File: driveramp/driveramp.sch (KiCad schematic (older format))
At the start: 91 parts, among them J1 SMA, J2 SMA, K1 CONN_3, K2 CONN_3, P2 CONN_2, Q1 BC547BTA, T1 MABACT0067, T2 2x Fair-Rite 2843006802, coax, U1 DG9411, U2 MRFE6VP100H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

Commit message: moved rf amps from control board to rxfe and driver
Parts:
- removed C1, C3: DNP, SMD_Packages:SMD-1210, symbol C
- removed C2: JMP, SMD_Packages:SMD-1210, symbol C
- removed C28, C39, C9: 100 nF, SMD_Packages:SMD-0805, symbol C
- removed K2: CONN_3, localconn:3-647166-3, symbol CONN_3
- removed R17, R18: DNP, SMD_Packages:SMD-0805, symbol R
- removed R19: 20, SMD_Packages:SMD-0805, symbol R
- removed R20: 52.3K 1%, SMD_Packages:SMD-0603, symbol R
- removed R21: 10K 1%, SMD_Packages:SMD-0603, symbol R
- removed R22: 10k, SMD_Packages:SMD-0603, symbol R
- removed U5: LT3010EMS8E, local:MSOP8-EP, symbol LT3010EMS8E
- added C? (x2): 22nF, SMD_Packages:SMD-0805, symbol C
- added C?: 100 nF, SMD_Packages:SMD-0805, symbol C
- added JP?: JUMPER3, symbol JUMPER3
- added L?: 1.5 uH, SMD_Packages:SM1812, symbol INDUCTOR
- added R?: 43.2, SMD_Packages:SM2512, symbol R
- added U?: GALI6+, symbol HMC475
- added U?: LM2937, symbol LM2937
- C20, C22: value 22nF -> DNP
- C24: value 100 pF -> 22 pF
- C26: value 10 nF -> 22 nF
- C38: value 1uF -> 10 uF
- C40: value 1uF 100V -> 100 nF
- R14: value 10k 1% -> 10k
- R15: value 1.5 -> 5.1
- R5: value 100k -> 10k
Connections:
- net labels added: VPP
- wire segments 197 -> 183
- no-connect marks 1 -> 0
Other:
- note added: "add GALI 6+ (12.2 dB gain)\nRemove amplifier from control board, cut bias on driver amp\nadd 15V input"
- note added: "jumper to \nselect pulsed/cw bias"
- note removed: "mouser cart:\nhttp://www.mouser.com/ProjectManager/ProjectDetail.aspx?AccessID=78a24cbee4\n\nDigikey: \nWeb ID 106262028 Access ID 70481"
- moved on the sheet: C38, C40, J1, L4, R16

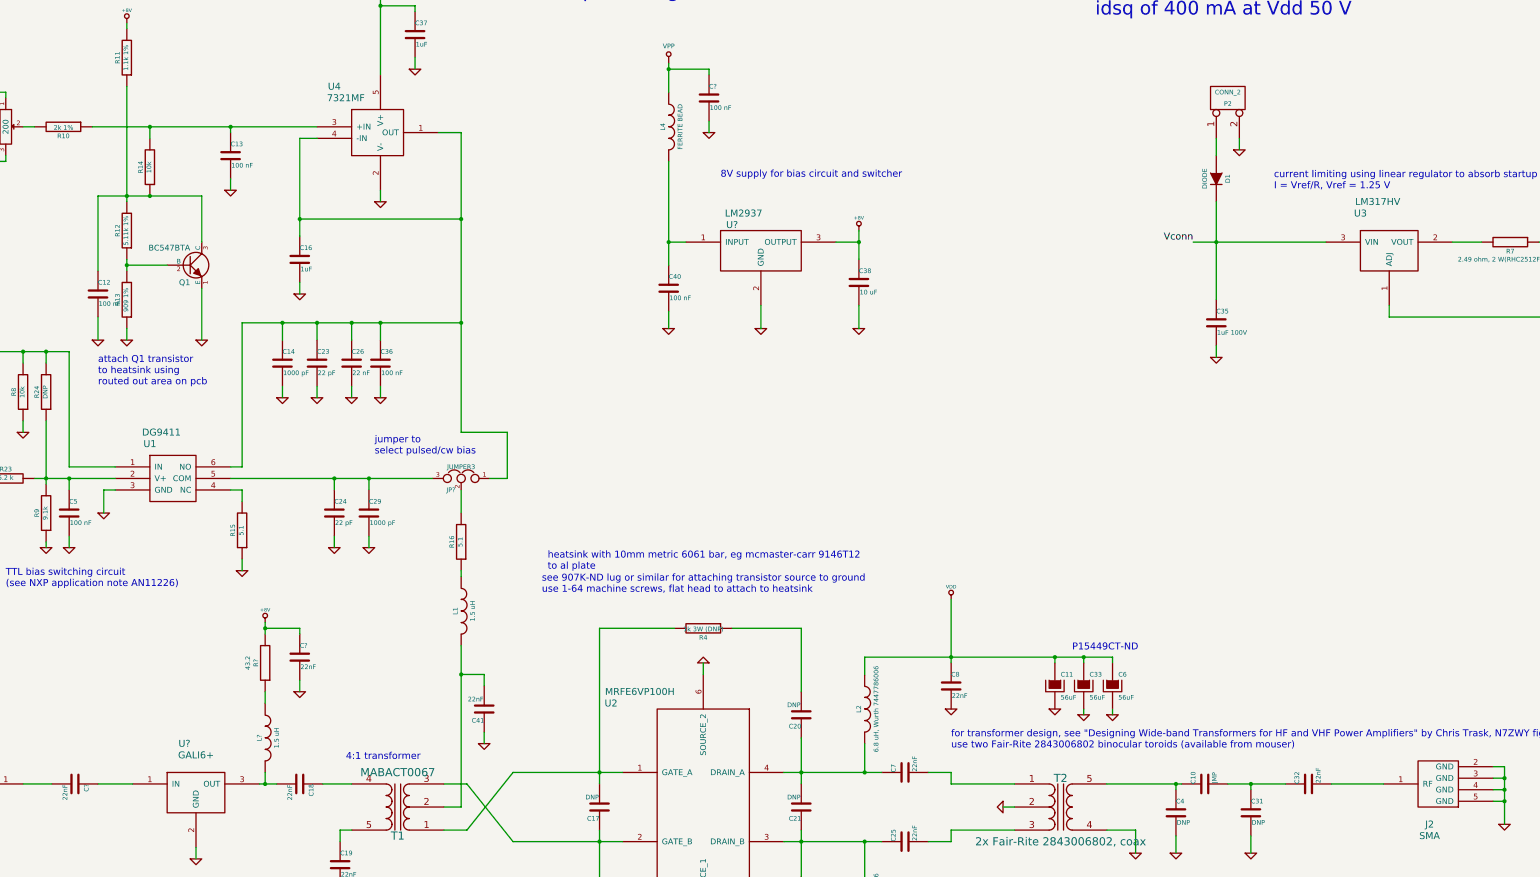
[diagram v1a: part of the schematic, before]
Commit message: DFM changes to boards - added fiducial markers and increase paste clearance
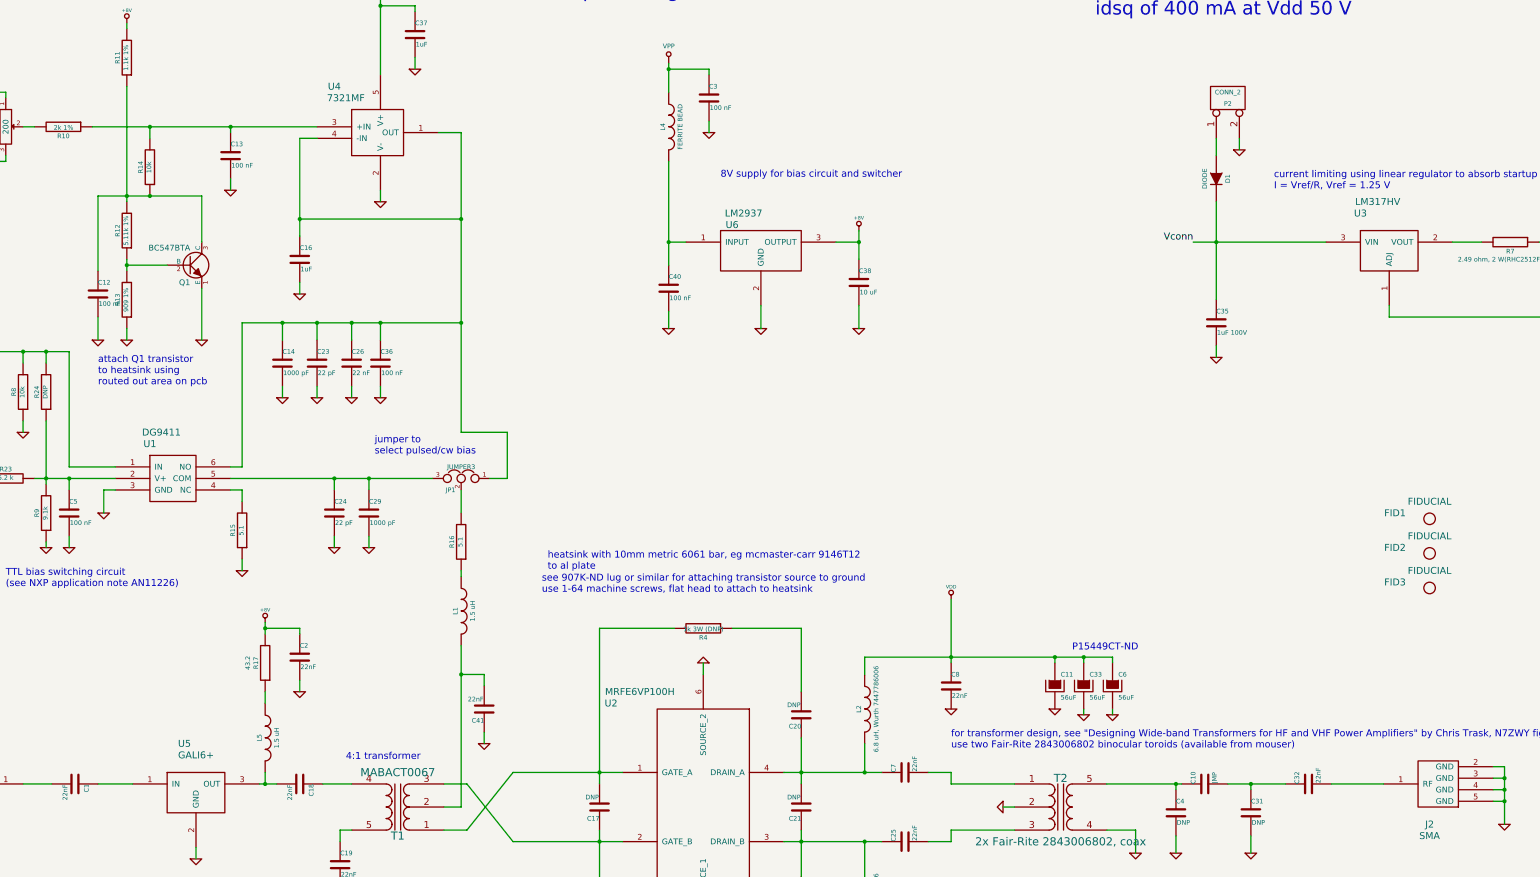
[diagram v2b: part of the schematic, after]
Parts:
- added FID1, FID2, FID3: FIDUCIAL, Mounting_Holes:MountingHole_2-7mm, symbol MOUNTING_HOLE
- gave numbers to parts that had none: 8

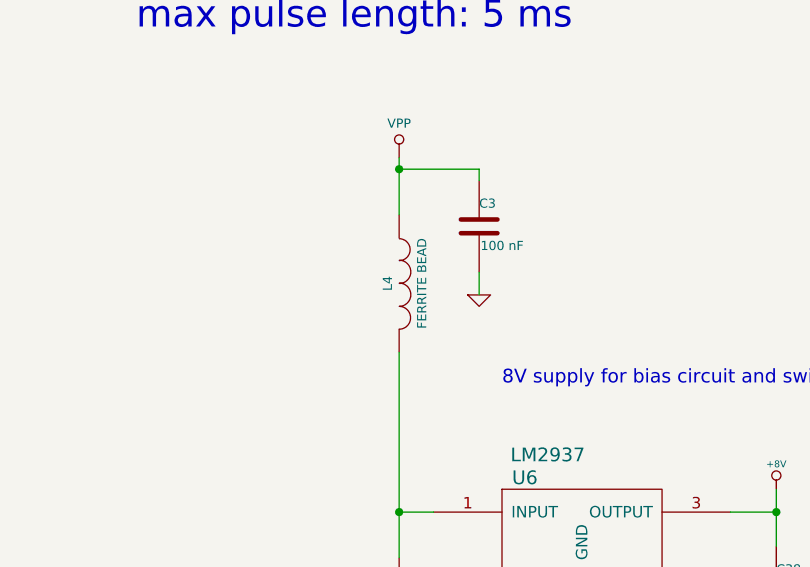
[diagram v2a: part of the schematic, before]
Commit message: finished layout of DFM'ed driver ampifier board.. except still need to change connectors
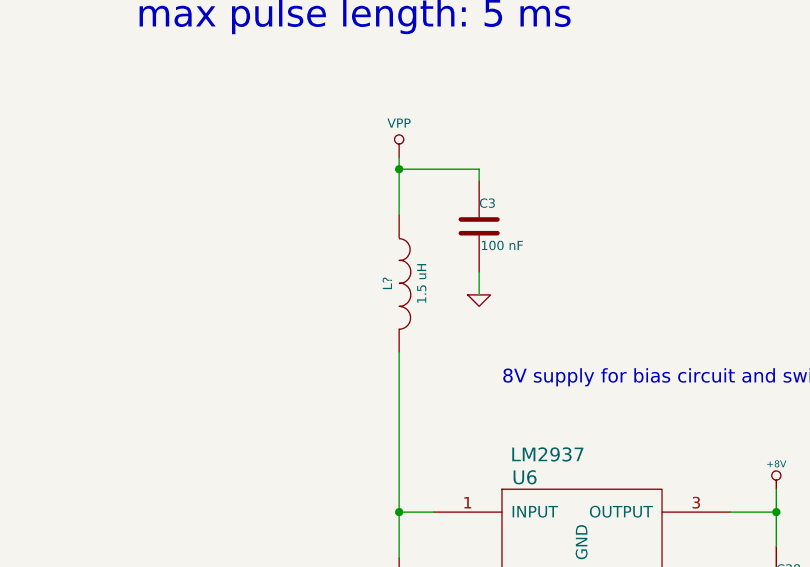
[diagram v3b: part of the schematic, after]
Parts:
- removed L4: FERRITE BEAD, SMD_Packages:SMD-0805, symbol INDUCTOR
- added L?: 1.5 uH, SMD_Packages:SMD-1812, symbol INDUCTOR
- C4: footprint SMD_Packages:SMD-1210 -> SMD_Packages:SMD-0805
- FID1, FID2, FID3: footprint Mounting_Holes:MountingHole_2-7mm -> sdtransmitter:FID_1MM
- JP1: footprint (none) -> localconn:3-647166-3
- L5: footprint SMD_Packages:SM1812 -> SMD_Packages:SMD-1812
- R17: footprint SMD_Packages:SM2512 -> SMD_Packages:SMD-0805
- U5: footprint (none) -> Housings_SOT-89:SOT89-3_Housing
- U6: footprint (none) -> SMD_Packages:SOT-223
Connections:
- net VPP: now also L?.1
- net at C40.1, U6.1 (INPUT): now also L?.2

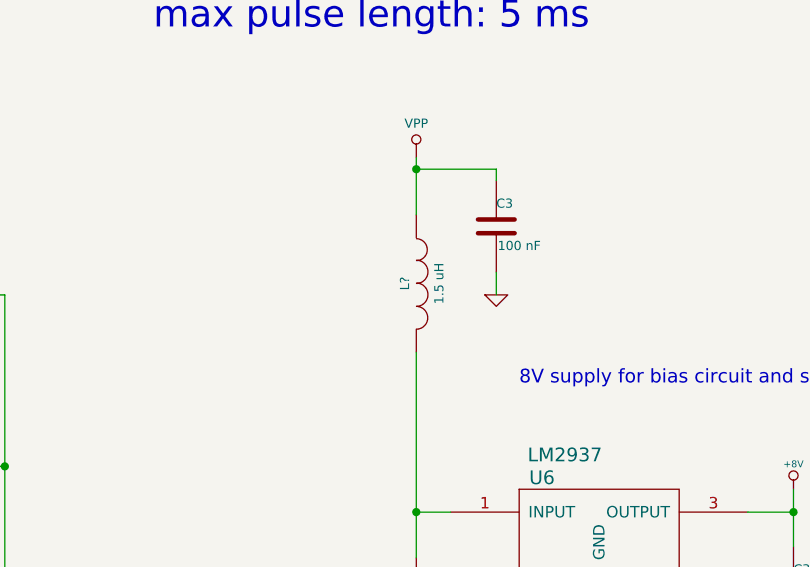
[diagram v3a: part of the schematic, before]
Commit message: changed all 3 pin headers to molex smd connectors available in tube packaging..
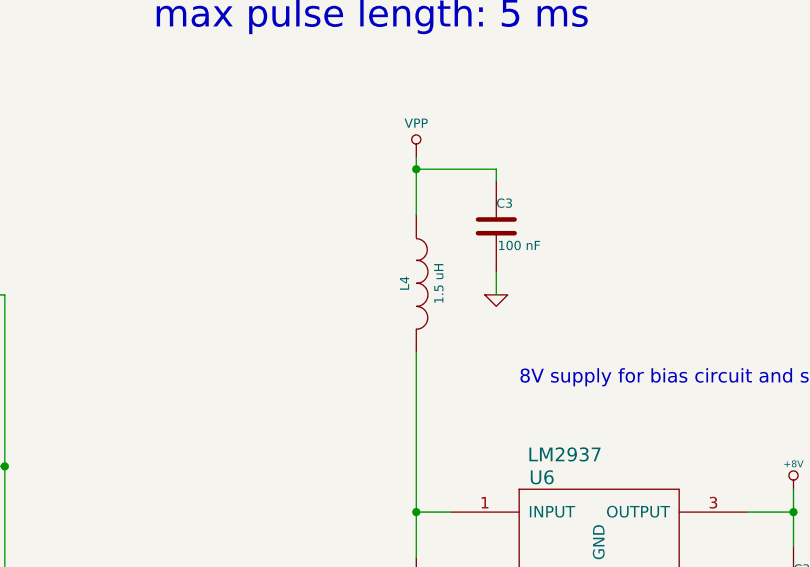
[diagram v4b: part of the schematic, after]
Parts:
- gave numbers to parts that had none: 1

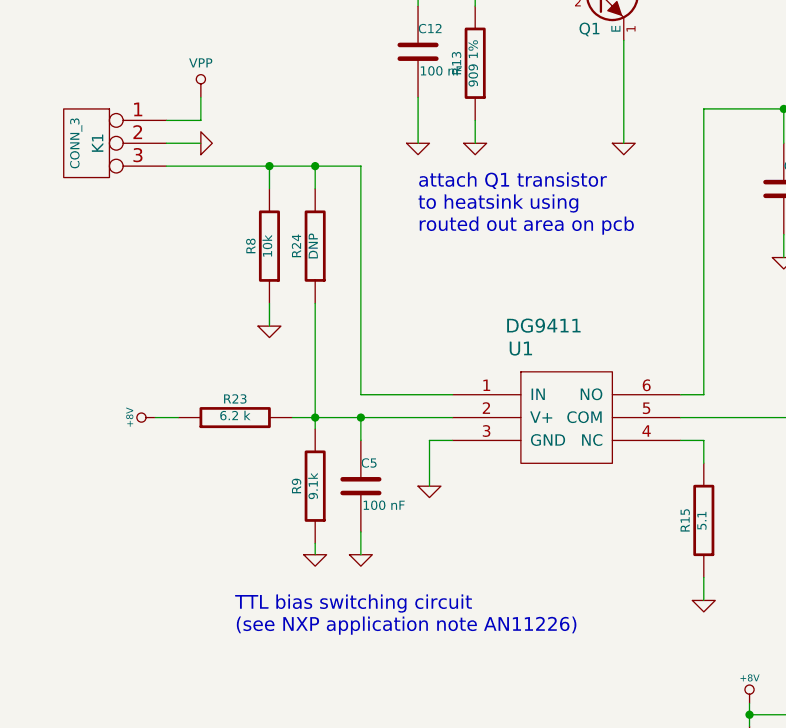
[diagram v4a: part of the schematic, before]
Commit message: rearranged high power T/R switch to place all connectors on one side for easier mounting to cases
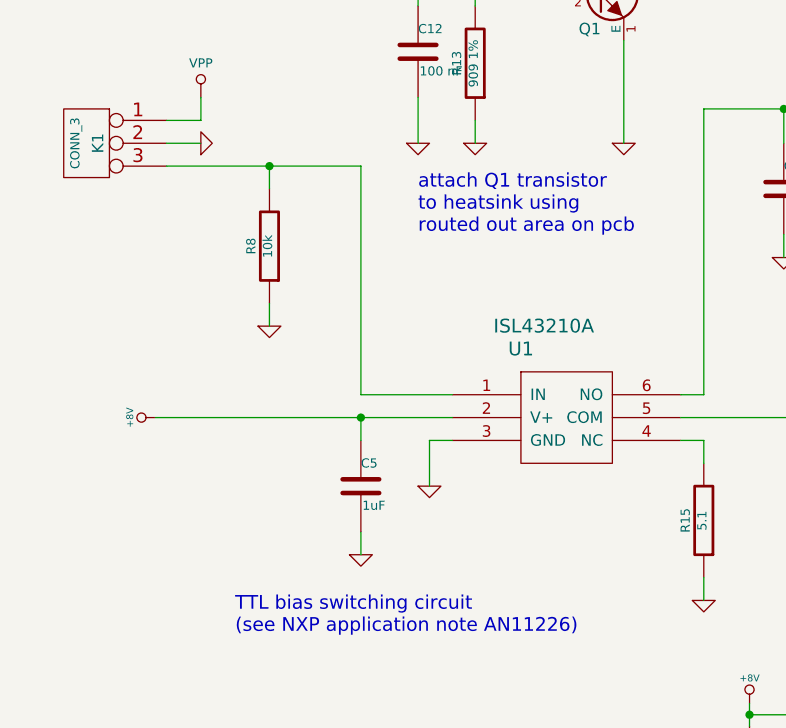
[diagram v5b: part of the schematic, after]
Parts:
- removed R23: 6.2 k, SMD_Packages:SMD-0603, symbol R
- removed R24: DNP, SMD_Packages:SMD-0603, symbol R
- removed R9: 9.1k, SMD_Packages:SMD-0603, symbol R
- C5: value 100 nF -> 1uF
- U1: value DG9411 -> ISL43210A
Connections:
- net +8V: now also C5.1, U1.2 (V+)
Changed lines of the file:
@@
 P 2900 5100
 F 0 "U1" H 2700 5400 60  0000 C CNN
-F 1 "DG9411" H 2800 5500 60  0000 C CNN
+F 1 "ISL43210A" H 2800 5500 60  0000 C CNN
 F 2 "Transistors_SMD:sc70-6" H 2900 5100 60  0001 C CNN
 F 3 "" H 2900 5100 60  0000 C CNN
@@
 P 2000 5400
 F 0 "C5" H 2000 5500 40  0000 L CNN
-F 1 "100 nF" H 2006 5315 40  0000 L CNN
+F 1 "1uF" H 2006 5315 40  0000 L CNN
 F 2 "SMD_Packages:SMD-0805" H 2038 5250 30  0001 C CNN
 F 3 "~" H 2000 5400 60  0000 C CNN
@@
 	1    2000 5700
 	1    0    0    -1
-$EndComp
-$Comp
-L R R9
-U 1 1 54ACADEE
-P 1800 5400
-F 0 "R9" V 1880 5400 40  0000 C CNN
-F 1 "9.1k" V 1807 5401 40  0000 C CNN
-F 2 "SMD_Packages:SMD-0603" V 1730 5400 30  0001 C CNN
-F 3 "" H 1800 5400 30  0000 C CNN
-	1    1800 5400
-	-1   0    0    1
-$EndComp
-$Comp
-L GND #PWR8
-U 1 1 54ACADF9
-P 1800 5700
-F 0 "#PWR8" H 1800 5700 30  0001 C CNN
-F 1 "GND" H 1800 5630 30  0001 C CNN
-F 2 "" H 1800 5700 60  0000 C CNN
-F 3 "" H 1800 5700 60  0000 C CNN
-	1    1800 5700
-	1    0    0    -1
-$EndComp
-$Comp
-L R R23
-U 1 1 54ACB329
-P 1450 5100
-F 0 "R23" V 1530 5100 40  0000 C CNN
-F 1 "6.2 k" V 1457 5101 40  0000 C CNN
-F 2 "SMD_Packages:SMD-0603" V 1380 5100 30  0001 C CNN
-F 3 "" H 1450 5100 30  0000 C CNN
-	1    1450 5100
-	0    -1   -1   0
 $EndComp
 $Comp
@@
 $EndComp
 $Comp
-L R R24
-U 1 1 54AF0A14
-P 1800 4350
-F 0 "R24" V 1880 4350 40  0000 C CNN
-F 1 "DNP" V 1807 4351 40  0000 C CNN
-F 2 "SMD_Packages:SMD-0603" V 1730 4350 30  0001 C CNN
-F 3 "" H 1800 4350 30  0000 C CNN
-	1    1800 4350
-	-1   0    0    1
-$EndComp
-$Comp
 L C C41
 U 1 1 54AF1275
@@
 	2000 4000 2000 5000
 Wire Wire Line
-	1700 5100 2400 5100
-Wire Wire Line
-	1800 4600 1800 5150
+	1100 5100 2400 5100
 Wire Wire Line
 	2000 5200 2000 5100
@@
 	2000 5600 2000 5700
 Wire Wire Line
-	1800 5650 1800 5700
-Connection ~ 1800 5100
-Wire Wire Line
-	1100 5100 1200 5100
-Wire Wire Line
 	1600 4700 1600 4600
 Wire Wire Line
@@
 	11950 2300 11950 2150
 Wire Wire Line
-	1800 4000 1800 4100
-Connection ~ 1800 4000
-Wire Wire Line
 	5400 6800 5600 6800

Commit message: cleanups on tr silkscreen, added fault header to driver amp
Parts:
- added K?: CONN_3, localconn:3-647166-3, symbol CONN_3
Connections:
- net GND: now also K?.1 (P1), K?.3 (P3)
- new net ~FAULT: K?.2 (PM)
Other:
- moved on the sheet: C1, C18, C2, L5, R17, U5
